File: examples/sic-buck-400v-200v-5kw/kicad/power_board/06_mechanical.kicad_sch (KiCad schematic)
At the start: 22 parts

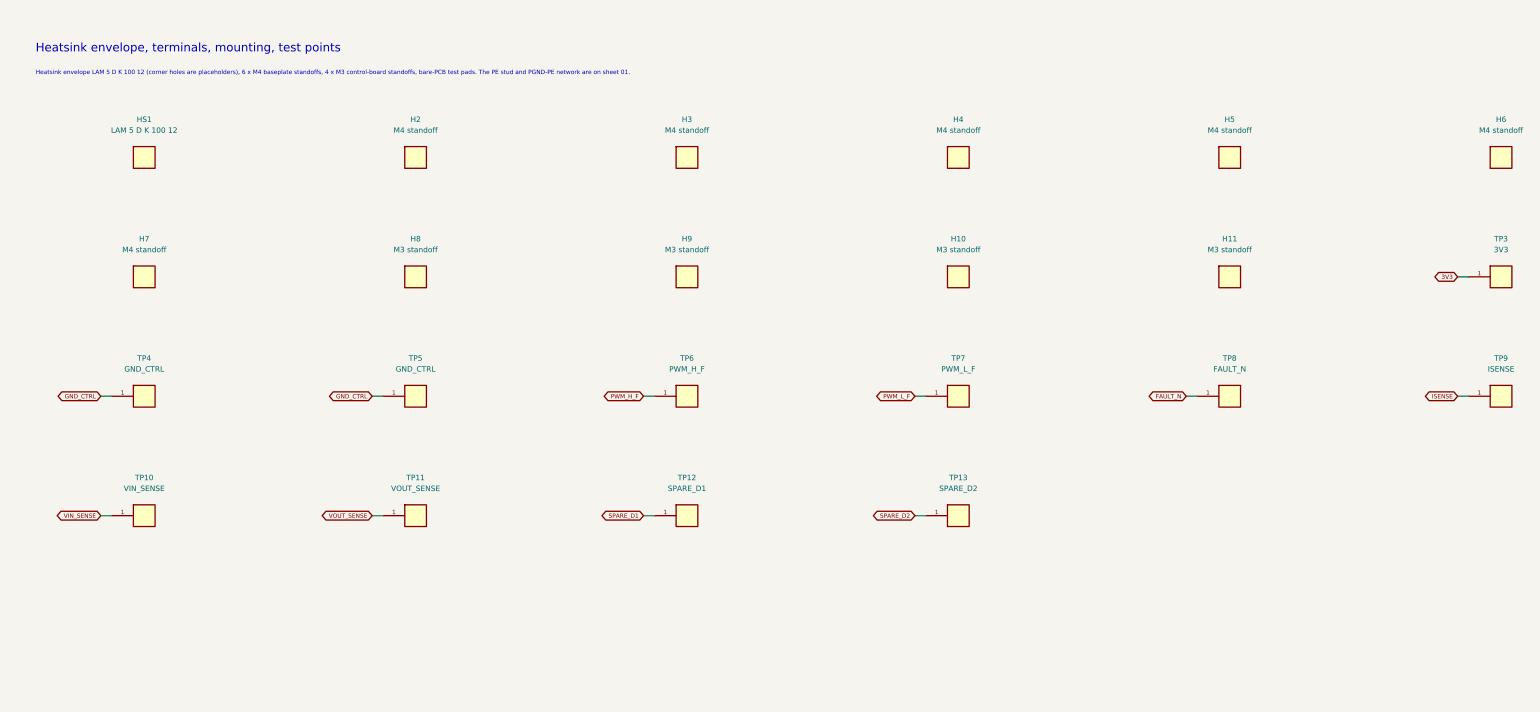
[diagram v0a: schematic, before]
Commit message: feat(v2.1): example regenerated - wired schematics, both boards routed with the upgraded router, exports, crops, validation
Schematics (wired style, gates passed): ERC 0 on both projects (power 20261012T075113Z-erc-df18ce6e,
control 20261012T075120Z-erc-7a14cacb); netlist (ref,pad)->net exact vs the model and vs the frozen V2
netlists with equal net names; .kicad_dru / net_settings identical to the legacy generation; stub
global labels 648 -> 7 (power) and 667 -> 7 (control), wired pin share 0 -> 0.90 / 0.76, junctions,
hierarchical labels and power symbols introduced, continuation sheets removed; readability metrics
V2 vs V2.1 in engineering_checks/schematic_readability_*.

Power board (octilinear simplification + tangent arcs on the V2 search; 8-direction search kept
opt-in after attempt A left 2 connections open): 0 unresolved, DRC 0/0/0 (20261012T090308Z-drc-8fd50803),
segments 4755 -> 2991 + 145 arcs, 90-degree bends 3609 -> 1121, stair runs 382 -> 124, length
5744.6 -> 5545.6 mm, vias 606 = V2, no net longer / more vias / narrower. Control board: 0 unresolved,
DRC 0/0/0 (20261012T084327Z-drc-7f07f983), segments 5995 -> 4262 + 261 arcs, 90-degree bends
4069 -> 1233, stair runs 435 -> 144, length 7055.2 -> 6700.7 mm, vias 798 = V2, 96 nets shorter,
0 longer. FOOTPRINT.SetDNP for DNP parts (schematic parity), beautify anchors bound to off-grid vias
by copper overlap (path_geometry.connected_by_overlap), In2.Cu inner pass styled.

Exports 11/11 per board, renders and layer PDFs refreshed, high-resolution V2/V2.1 crops under
review/crops/, routing_quality_* and v21_validation.{json,md} (nine TASK 7 checks independently
re-derived). verify_sic_buck passed; 338 tests OK (2 skipped).

Co-Authored-By: Claude Fable 5.1 <noreply@anthropic.com>
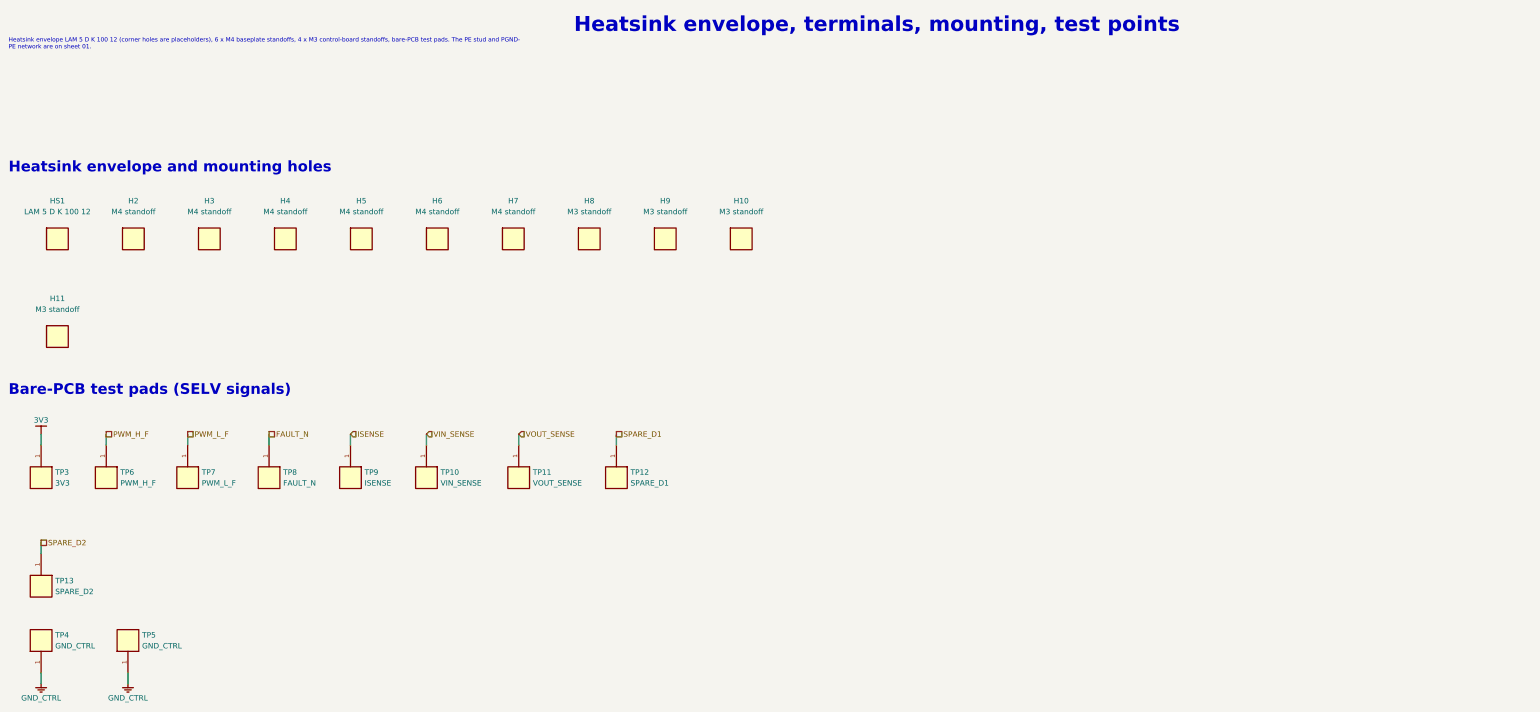
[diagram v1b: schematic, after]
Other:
- note added: "Bare-PCB test pads (SELV signals)"
- note added: "Heatsink envelope LAM 5 D K 100 12 (corner holes are placeholders), 6 x M4 baseplate standoffs, 4 x M3 control-board standoffs, bare-PCB test pads. The PE stud and PGND- PE network are on sheet 01."
- note added: "Heatsink envelope and mounting holes"
- note removed: "Heatsink envelope LAM 5 D K 100 12 (corner holes are placeholders), 6 x M4 baseplate standoffs, 4 x M3 control-board standoffs, bare-PCB test pads. The PE stud and PGND-PE network are on sheet 01."
- moved on the sheet: H10, H11, H2, H3, H4, H5, H6, H7, H8, H9, HS1, TP10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
